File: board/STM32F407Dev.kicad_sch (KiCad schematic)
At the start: 61 parts, among them J1 USB_C_Receptacle_USB2.0_16P, J2 Conn_01x08_MountingPin, J3 Conn_02x19_Odd_Even, J4 Conn_02x19_Odd_Even, J5 Conn_01x04, Q1 AO3401A, SW1 SW_Push, SW2 SW_Push, SW3 SW_Push, SW4 SW_Push, U1 STM32F407VGTx, U2 W25N01GVZE, U3 ME6211C33M5, Y1 24MHz, Y2 32.768kHz

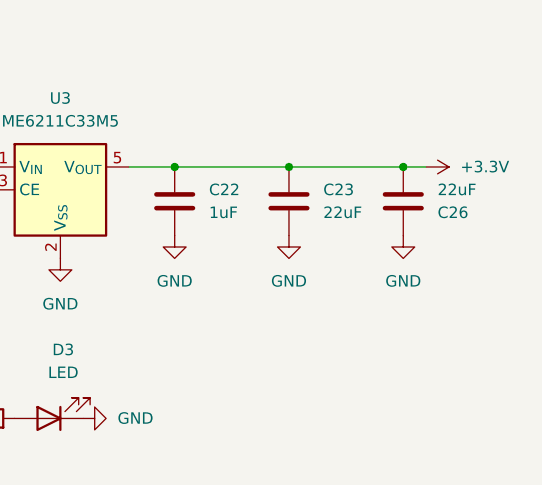
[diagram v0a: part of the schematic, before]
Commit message: Update STM32F407 file, delete backup and lock
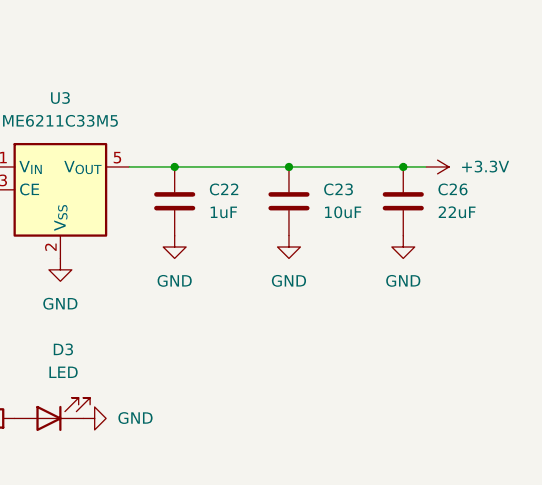
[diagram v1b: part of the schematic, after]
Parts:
- C23: value 22uF -> 10uF
- U2: footprint Package_SON:WSON-8-1EP_8x6mm_P1.27mm_EP3.4x4.3mm -> Cascade_SON:WSON-8-1EP_8x6mm_P1.27mm_EP3.4x4.3mm_WidePin; symbol Serial_Flash:W25N01GVZE -> Cascade_Flash:W25N01FGVZE
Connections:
- net +3.3V: now also C26.1; no longer C26.2
- net GND: now also C26.2; no longer C26.1
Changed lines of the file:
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@@
 	)
 	(junction
-		(at 368.3 35.56)
-		(diameter 0)
-		(color 0 0 0 0)
-	)
-	(junction
 		(at 109.22 27.94)
 		(diameter 0)
@@
 	)
 	(junction
+		(at 368.3 35.56)
+		(diameter 0)
+		(color 0 0 0 0)
+	)
+	(junction
 		(at 58.42 35.56)
 		(diameter 0)
@@
 	(wire
 		(pts
-			(xy 368.3 35.56) (xy 370.84 35.56)
-		)
-		(stroke
-			(width 0)
-			(type default)
-		)
-	)
-	(wire
-		(pts
 			(xy 101.6 186.69) (xy 101.6 184.15)
 		)
@@
 	(wire
 		(pts
+			(xy 368.3 35.56) (xy 370.84 35.56)
+		)
+		(stroke
+			(width 0)
+			(type default)
+		)
+	)
+	(wire
+		(pts
 			(xy 203.2 160.02) (xy 215.9 160.02)
 		)
@@
 	)
 	(symbol
-		(lib_id "Device:C")
-		(at 368.3 39.37 0)
-		(mirror x)
-		(unit 1)
-		(exclude_from_sim no)
-		(in_bom yes)
-		(on_board yes)
-		(dnp no)
-		(property "Reference" "C26"
-			(at 372.11 40.6401 0)
-			(effects
-				(font
-					(size 1.27 1.27)
-				)
-				(justify left)
-			)
-		)
-		(property "Value" "22uF"
-			(at 372.11 38.1001 0)
-			(effects
-				(font
-					(size 1.27 1.27)
-				)
-				(justify left)
-			)
-		)
-		(property "Footprint" "Capacitor_SMD:C_0805_2012Metric"
-			(at 369.2652 35.56 0)
-			(effects
-				(font
-					(size 1.27 1.27)
-				)
-				(hide yes)
-			)
-		)
-		(property "Datasheet" "~"
-			(at 368.3 39.37 0)
-			(effects
-				(font
-					(size 1.27 1.27)
-				)
-				(hide yes)
-			)
-		)
-		(property "Description" "Unpolarized capacitor"
-			(at 368.3 39.37 0)
-			(effects
-				(font
-					(size 1.27 1.27)
-				)
-				(hide yes)
-			)
-		)
-		(pin "2"
-		)
-		(pin "1"
-		)
-		(instances
-			(project "STM32F407Dev"
-				(path "/49dd0cbc-cf06-4110-9167-40afd4d5aa22"
-					(reference "C26")
-					(unit 1)
-				)
-			)
-		)
-	)
-	(symbol
 		(lib_id "power:GND")
 		(at 58.42 172.72 0)
@@
 			)
 		)
-		(property "Value" "22uF"
+		(property "Value" "10uF"
 			(at 359.41 40.6399 0)
 			(effects
@@
 	)
 	(symbol
-		(lib_id "Serial_Flash:W25N01GVZE")
+		(lib_id "Cascade_Flash:W25N01FGVZE")
 		(at 203.2 177.8 0)
 		(unit 1)
@@
 			)
 		)
-		(property "Footprint" "Package_SON:WSON-8-1EP_8x6mm_P1.27mm_EP3.4x4.3mm"
-			(at 198.12 170.18 0)
+		(property "Footprint" "Cascade_SON:WSON-8-1EP_8x6mm_P1.27mm_EP3.4x4.3mm_WidePin"
+			(at 203.2 177.8 0)
 			(effects
 				(font
@@
 		)
 		(property "Datasheet" "https://www.winbond.com/resource-files/W25N01GV%20Rev%20R%20070323.pdf"
-			(at 198.12 170.18 0)
+			(at 203.2 177.8 0)
 			(effects
 				(font
@@
 		)
 		(property "Description" "3V 1Gbit Serial SLC NAND Flash Memory, Dual/Quad SPI, Buffer Read & Continous Read"
-			(at 198.12 170.18 0)
+			(at 203.2 177.8 0)
 			(effects
 				(font
@@
 					(unit 1)
 				)
+			)
+		)
+	)
+	(symbol
+		(lib_id "Device:C")
+		(at 368.3 39.37 0)
+		(unit 1)
+		(exclude_from_sim no)
+		(in_bom yes)
+		(on_board yes)
+		(dnp no)
+		(fields_autoplaced yes)
+		(property "Reference" "C26"
+			(at 372.11 38.0999 0)
+			(effects
+				(font
+					(size 1.27 1.27)
+				)
+				(justify left)
+			)
+		)
+		(property "Value" "22uF"
+			(at 372.11 40.6399 0)
+			(effects
+				(font
+					(size 1.27 1.27)
+				)
+				(justify left)
+			)
+		)
+		(property "Footprint" "Capacitor_SMD:C_0805_2012Metric"
+			(at 369.2652 43.18 0)
+			(effects
+				(font
+					(size 1.27 1.27)
+				)
+				(hide yes)
+			)
+		)
+		(property "Datasheet" "~"
+			(at 368.3 39.37 0)
+			(effects
+				(font
+					(size 1.27 1.27)
+				)
+				(hide yes)
+			)
+		)
+		(property "Description" "Unpolarized capacitor"
+			(at 368.3 39.37 0)
+			(effects
+				(font
+					(size 1.27 1.27)
+				)
+				(hide yes)
+			)
+		)
+		(pin "2"
+		)
+		(pin "1"
+		)
+		(instances
+			(project "STM32F407Dev"
+				(path "/49dd0cbc-cf06-4110-9167-40afd4d5aa22"
+					(reference "C26")
+					(unit 1)
+				)
